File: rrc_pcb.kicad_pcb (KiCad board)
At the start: 2 copper layers, 148.8 x 62.4 mm, 20 parts, among them J1 Voltage Regulator Input, J2 Conn_01x03_Male, U1 ADXL357Z, U2 Teensy3.6-teensy, U3 BN220-GPS, U4 MS5611, U5 logo

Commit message: update 2
updated .sch added teensy4.1 , and updated footprints. Still in debugging stage
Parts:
- removed REF** (x7): MountingHole_2.1mm, MountingHole:MountingHole_2.1mm
- removed RF11: RFD900+-RF_Module, rfd900+:RFD900+
- added U6: logo, logo:RRC_logo, F.Cu at (152.4, 16.5)
- U1: value ADXL357Z -> iridium9602; footprint adxl357z:ADXL357 -> Connector_PinHeader_2.54mm:PinHeader_1x04_P2.54mm_Horizontal
- U2: value Teensy3.6-teensy -> DEV-16771; footprint teensy:Teensy35_36 -> teensy:Teensy41
- U4: value MS5611 -> ICM-20948; footprint ms5611:1x07 -> Connector_PinHeader_2.54mm:PinHeader_2x10_P2.54mm_Vertical
- U5: value logo -> MS5611; footprint logo:RRC_logo -> ms5611:1x07
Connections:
- R3 pad 1: Net-(R3-Pad1) -> SCL1
- R4 pad 1: Net-(R4-Pad1) -> SDA1
- U1 pad 2: unconnected-(U1-Pad2) -> TX2
- U1 pad 3: T_VCC -> RX2
- U1 pad 4: unconnected-(U1-Pad4) -> GND
- U2 pad 1: T_GND -> TX1
- U2 pad 11: Net-(RF11-Pad9) -> unconnected-(U2-Pad11)
- U2 pad 12: Net-(RF11-Pad7) -> unconnected-(U2-Pad12)
- U2 pad 15: T_VCC -> unconnected-(U2-Pad15)
- U2 pad 16: unconnected-(U2-Pad16) -> SCL1
- U2 pad 17: unconnected-(U2-Pad17) -> SDA1
- U2 pad 18: unconnected-(U2-Pad18) -> Net-(R2-Pad1)
- U2 pad 19: unconnected-(U2-Pad19) -> Net-(R1-Pad1)
- U2 pad 2: Net-(U2-Pad2) -> unconnected-(U2-Pad2)
- U2 pad 24: Net-(BZ1-Pad1) -> unconnected-(U2-Pad24)
- U2 pad 3: Net-(U2-Pad3) -> unconnected-(U2-Pad3)
- U2 pad 39: GND -> unconnected-(U2-Pad39)
- U2 pad 41: unconnected-(U2-Pad41) -> Net-(BZ1-Pad1)
- U2 pad 42: unconnected-(U2-Pad42) -> (no net)
- U2 pad 43: unconnected-(U2-Pad43) -> (no net)
- U2 pad 44: unconnected-(U2-Pad44) -> (no net)
- U2 pad 45: Net-(R2-Pad1) -> (no net)
- U2 pad 46: Net-(R1-Pad1) -> (no net)
- U2 pad 47: unconnected-(U2-Pad47) -> (no net)
- U2 pad 48: unconnected-(U2-Pad48) -> (no net)
- U2 pad 49: unconnected-(U2-Pad49) -> (no net)
- U2 pad 5: Net-(R3-Pad1) -> unconnected-(U2-Pad5)
- U2 pad 50: unconnected-(U2-Pad50) -> (no net)
- U2 pad 51: unconnected-(U2-Pad51) -> (no net)
- U2 pad 52: unconnected-(U2-Pad52) -> (no net)
- U2 pad 53: VCC -> (no net)
- U2 pad 54: unconnected-(U2-Pad54) -> (no net)
- U2 pad 55: unconnected-(U2-Pad55) -> (no net)
- U2 pad 56: unconnected-(U2-Pad56) -> (no net)
- U2 pad 57: unconnected-(U2-Pad57) -> (no net)
- U2 pad 6: Net-(R4-Pad1) -> unconnected-(U2-Pad6)
- U2 pad 7: unconnected-(U2-Pad7) -> RX2
- U2 pad 8: unconnected-(U2-Pad8) -> TX2
- U3 pad 2: Net-(U2-Pad3) -> TX1
- U3 pad 3: Net-(U2-Pad2) -> RX1
- U4 pad 1: T_VCC -> unconnected-(U4-Pad1)
- U4 pad 2: T_GND -> unconnected-(U4-Pad2)
- U4 pad 3: Net-(R3-Pad1) -> unconnected-(U4-Pad3)
- U4 pad 4: Net-(R4-Pad1) -> unconnected-(U4-Pad4)
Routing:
- net unconnected-(U2-Pad34): track 0.00 -> 163.4 mm
- net GND: track 163.4 -> 0.00 mm
- net unconnected-(U2-Pad11): track 0.00 -> 108.6 mm
- net Net-(RF11-Pad9): track 108.6 -> 0.00 mm
- net unconnected-(U2-Pad12): track 0.00 -> 108.5 mm
- net Net-(RF11-Pad7): track 108.5 -> 0.00 mm
- net Net-(BZ1-Pad1): track 84.5 -> 191.7 mm
- net Net-(R1-Pad1): track 107.2 -> 0.00 mm
- net SDA1: track 0.00 -> 94.0 mm
- net Net-(R4-Pad1): track 48.8 -> 0.00 mm
- net Net-(R3-Pad1): track 45.2 -> 0.00 mm
- net unconnected-(U2-Pad2): track 0.00 -> 25.8 mm, vias 0 -> 1
- net Net-(U2-Pad2): track 25.8 -> 0.00 mm, vias 1 -> 0
- net unconnected-(U2-Pad3): track 0.00 -> 25.3 mm
- net Net-(U2-Pad3): track 25.3 -> 0.00 mm
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
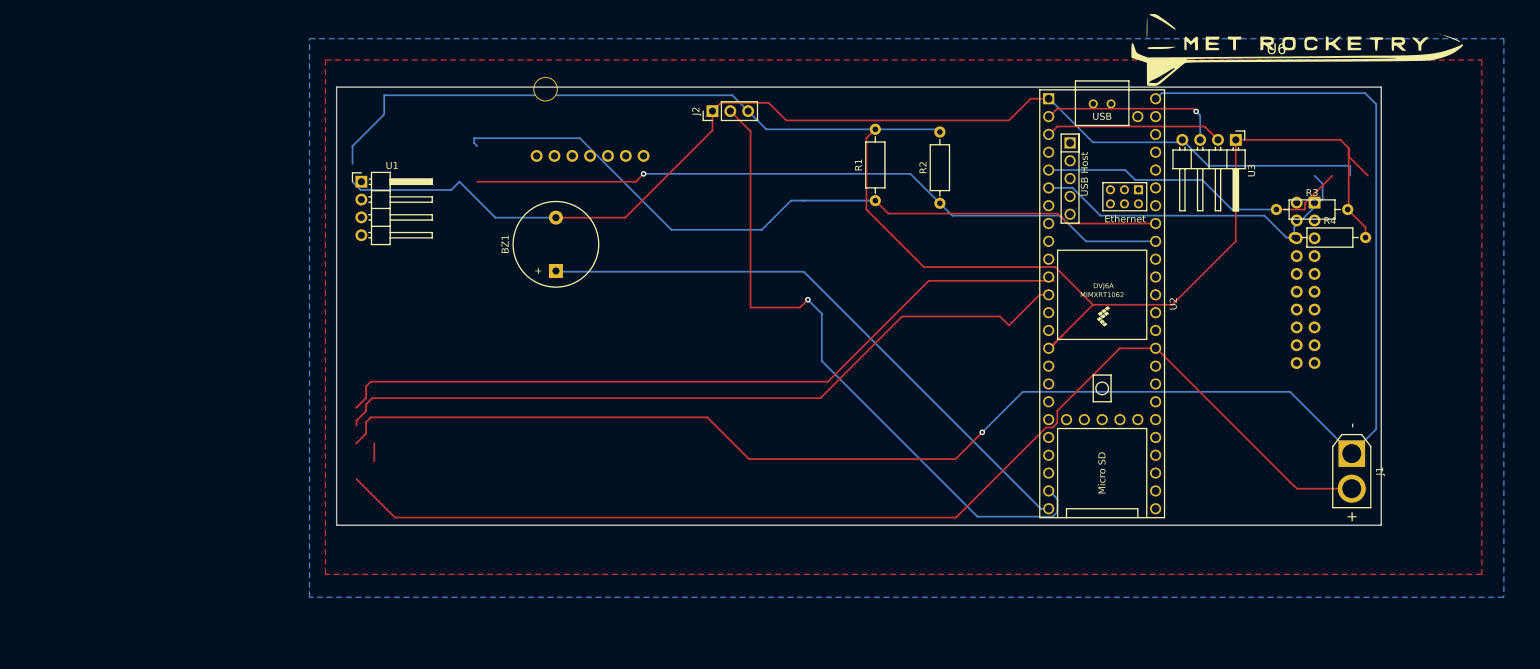
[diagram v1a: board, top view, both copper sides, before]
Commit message: updated pcb footprints
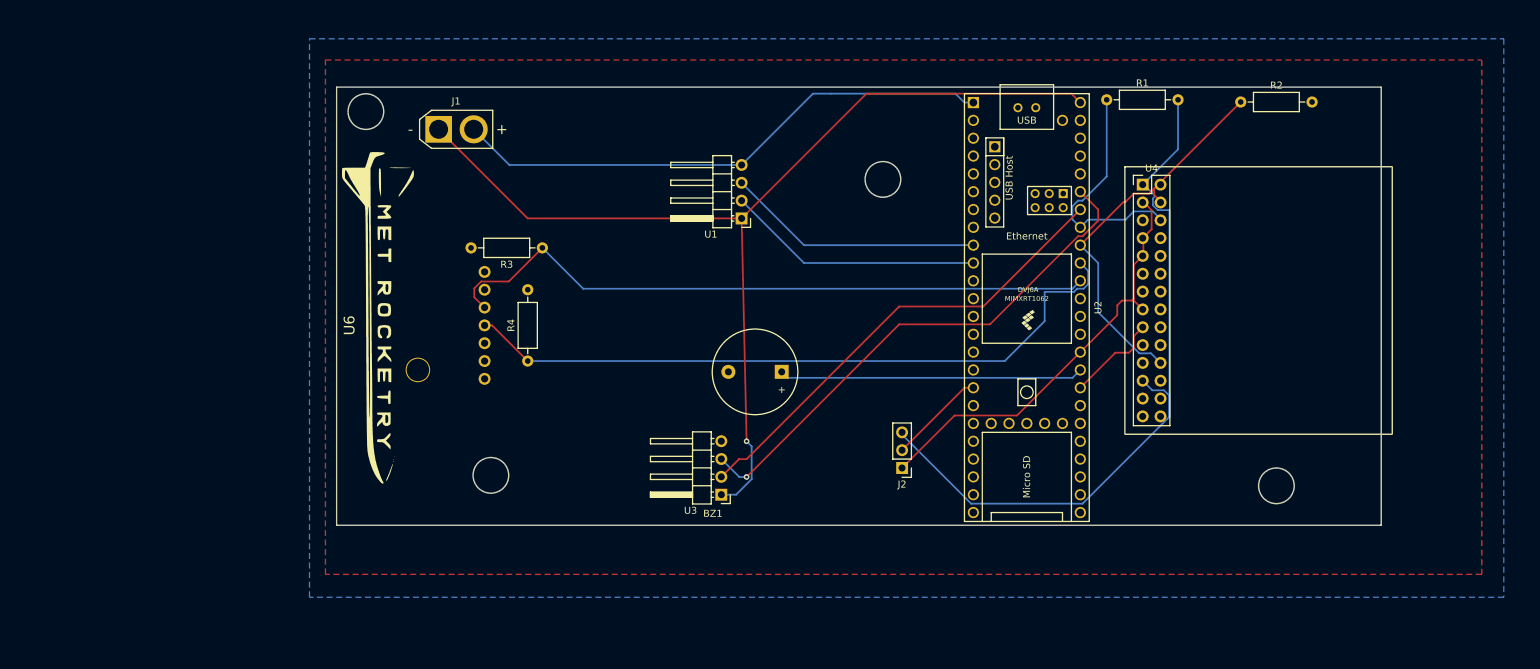
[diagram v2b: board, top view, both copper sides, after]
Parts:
- BZ1: value Buzzer -> Buzzer-Device
- J1: value Voltage Regulator Input -> Conn_01x02_Male-Connector
- J2: value Conn_01x03_Male -> Conn_01x03_Male-Connector
- R1, R2, R3, R4: value Pull up -> R-Device
- U2: value DEV-16771 -> Teensy4.1
- U4: value ICM-20948 -> ICM-20948; footprint Connector_PinHeader_2.54mm:PinHeader_2x10_P2.54mm_Vertical -> Connector_PinHeader_2.54mm:PinHeader_2x14_P2.54mm_Vertical; moved to F.Cu
- moved J1 138.1 mm to (33.0, 27.9), turned to 0 degrees
- moved U6 132.7 mm to (24.5, 51.9), turned to -90 degrees
- moved R4 110.6 mm to (45.7, 61.0), turned to 90 degrees
- moved R3 104.7 mm to (47.8, 44.8), turned to 180 degrees
- moved U3 89.1 mm to (73.3, 80.0), turned to 180 degrees
- moved J2 57.6 mm to (99.1, 76.2), turned to 180 degrees
- moved U1 54.4 mm to (76.2, 40.6), turned to 180 degrees
- moved R2 45.2 mm to (147.3, 24.1), turned to 0 degrees
- moved R1 36.0 mm to (128.2, 23.7), turned to 0 degrees
- moved BZ1 35.2 mm to (81.9, 62.5), turned to 180 degrees
- moved U4 24.6 mm to (133.3, 35.8), turned to 0 degrees
- moved U5 23.2 mm to (43.4, 55.9), turned to -90 degrees
- moved U2 10.7 mm to (116.8, 53.3)
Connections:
- R1 pad 1: Net-(R1-Pad1) -> SCL2
- R2 pad 1: Net-(R2-Pad1) -> SDA2
- U1 pad 1: T_VCC -> VCC
- U2 pad 1: TX1 -> GND
- U2 pad 10: unconnected-(U2-Pad10) -> TX2
- U2 pad 15: unconnected-(U2-Pad15) -> T_VCC
- U2 pad 16: SCL1 -> unconnected-(U2-Pad16)
- U2 pad 17: SDA1 -> Net-(J2-Pad2)
- U2 pad 18: Net-(R2-Pad1) -> unconnected-(U2-Pad18)
- U2 pad 19: Net-(R1-Pad1) -> unconnected-(U2-Pad19)
- U2 pad 23: Net-(J2-Pad2) -> unconnected-(U2-Pad23)
- U2 pad 32: unconnected-(U2-Pad32) -> INT1
- U2 pad 33: unconnected-(U2-Pad33) -> Net-(BZ1-Pad1)
- U2 pad 34: unconnected-(U2-Pad34) -> T_GND
- U2 pad 38: unconnected-(U2-Pad38) -> SCL1
- U2 pad 39: unconnected-(U2-Pad39) -> SDA1
- U2 pad 40: unconnected-(U2-Pad40) -> SDA2
- U2 pad 41: Net-(BZ1-Pad1) -> SCL2
- U2 pad 42: (no net) -> TX1
- U2 pad 43: (no net) -> RX1
- U2 pad 44: (no net) -> unconnected-(U2-Pad44)
- U2 pad 45: (no net) -> unconnected-(U2-Pad45)
- U2 pad 46: (no net) -> unconnected-(U2-Pad46)
- U2 pad 47: (no net) -> unconnected-(U2-Pad47)
- U2 pad 48: (no net) -> VCC
- U2 pad 49: (no net) -> unconnected-(U2-Pad49)
- U2 pad 50: (no net) -> unconnected-(U2-Pad50)
- U2 pad 51: (no net) -> unconnected-(U2-Pad51)
- U2 pad 52: (no net) -> unconnected-(U2-Pad52)
- U2 pad 53: (no net) -> unconnected-(U2-Pad53)
- U2 pad 54: (no net) -> unconnected-(U2-Pad54)
- U2 pad 55: (no net) -> unconnected-(U2-Pad55)
- U2 pad 56: (no net) -> unconnected-(U2-Pad56)
- U2 pad 57: (no net) -> unconnected-(U2-Pad57)
- U2 pad 58: (no net) -> unconnected-(U2-Pad58)
- U2 pad 59: (no net) -> unconnected-(U2-Pad59)
- U2 pad 60: (no net) -> unconnected-(U2-Pad60)
- U2 pad 61: (no net) -> unconnected-(U2-Pad61)
- U2 pad 62: (no net) -> unconnected-(U2-Pad62)
- U2 pad 63: (no net) -> unconnected-(U2-Pad63)
- U2 pad 64: (no net) -> unconnected-(U2-Pad64)
- U2 pad 65: (no net) -> unconnected-(U2-Pad65)
- U2 pad 66: (no net) -> unconnected-(U2-Pad66)
- U2 pad 67: (no net) -> unconnected-(U2-Pad67)
- U2 pad 7: RX2 -> unconnected-(U2-Pad7)
- U2 pad 8: TX2 -> unconnected-(U2-Pad8)
- U2 pad 9: unconnected-(U2-Pad9) -> RX2
- U3 pad 1: T_VCC -> VCC
- U4 pad 13: T_VCC -> unconnected-(U4-Pad13)
- U4 pad 15: unconnected-(U4-Pad15) -> T_GND
- U4 pad 17: unconnected-(U4-Pad17) -> T_GND
- U4 pad 18: T_GND -> unconnected-(U4-Pad18)
- U4 pad 19: T_GND -> unconnected-(U4-Pad19)
- U4 pad 20: T_GND -> SCL2
- U4 pad 7: unconnected-(U4-Pad7) -> INT1
- U4 pad 8: T_VCC -> unconnected-(U4-Pad8)
- U4 pad 9: unconnected-(U4-Pad9) -> (no net)
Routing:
- net unconnected-(U2-Pad34): track 163.4 -> 0.00 mm
- net Net-(BZ1-Pad1): track 191.7 -> 43.4 mm
- net T_VCC: track 228.3 -> 105.3 mm
- net unconnected-(U2-Pad11): track 108.6 -> 0.00 mm
- net unconnected-(U2-Pad12): track 108.5 -> 0.00 mm
- net Net-(R2-Pad1): track 101.2 -> 0.00 mm, vias 1 -> 0
- net T_GND: track 161.6 -> 61.2 mm
- net SCL1: track 0.00 -> 95.0 mm
- net VCC: track 237.9 -> 147.3 mm
- net Net-(J2-Pad2): track 93.9 -> 13.8 mm, vias 1 -> 0
- net GND: track 0.00 -> 78.0 mm
- net RX1: track 0.00 -> 75.1 mm, vias 0 -> 1
- net TX1: track 0.00 -> 66.9 mm
- net SDA2: track 0.00 -> 56.1 mm
- net TX2: track 0.00 -> 36.7 mm
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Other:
- outline, holes or cut-outs redrawn

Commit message: optimized and finalized pcb
reduced sizing and fixed traces.
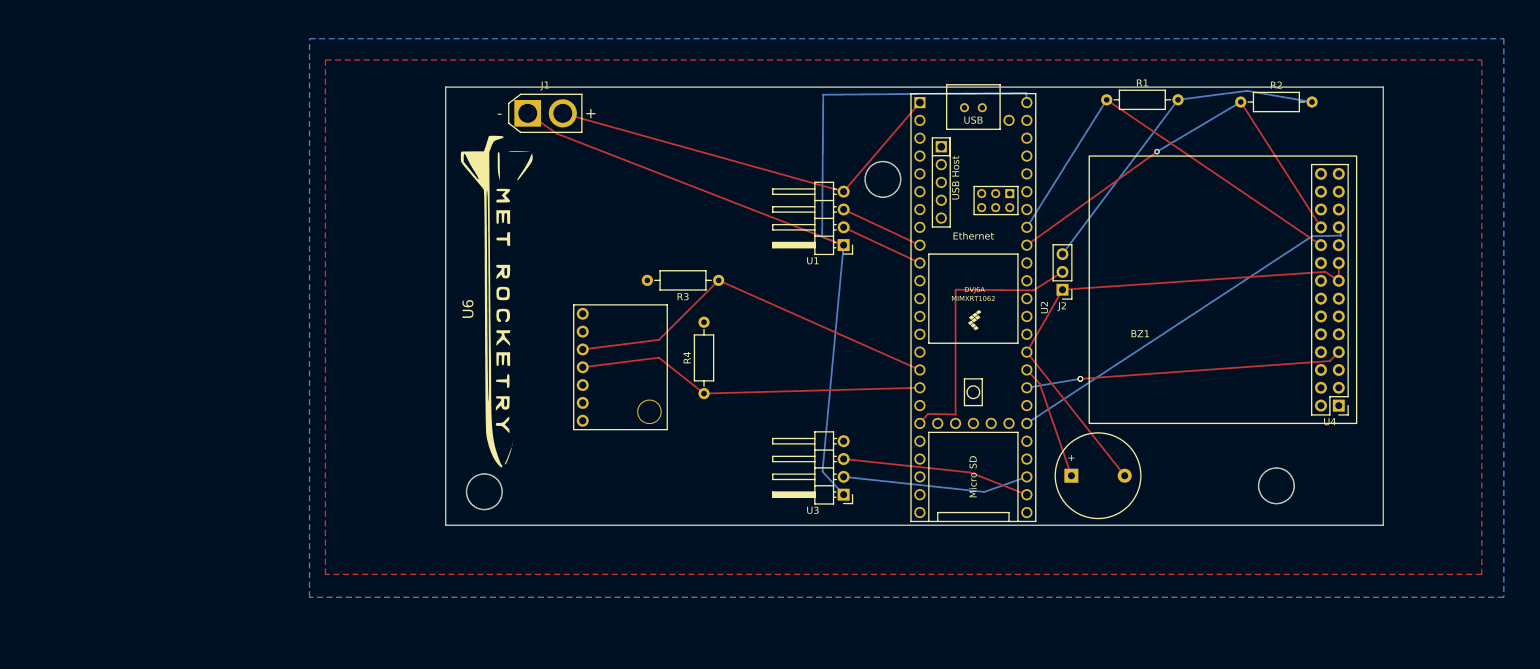
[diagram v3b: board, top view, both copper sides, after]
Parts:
- U5: moved to F.Cu
- moved BZ1 43.9 mm to (123.2, 77.3), turned to 0 degrees
- moved U4 42.1 mm to (161.3, 67.3), turned to 180 degrees
- moved J2 34.2 mm to (121.9, 50.8)
- moved R3 25.5 mm to (72.9, 49.5)
- moved R4 25.5 mm to (70.8, 65.6)
- moved U3 17.4 mm to (90.7, 80.0)
- moved U6 17.1 mm to (41.4, 49.5)
- moved U1 15.0 mm to (90.7, 44.4)
- moved J1 12.9 mm to (45.7, 25.7)
- moved U5 8.70 mm to (49.7, 61.8)
- moved U2 7.62 mm to (109.2, 53.3)
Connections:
- J2 pad 2: Net-(J2-Pad2) -> Net-(U2-Pad19)
- U2 pad 16: unconnected-(U2-Pad16) -> SCL1
- U2 pad 17: Net-(J2-Pad2) -> SDA1
- U2 pad 19: unconnected-(U2-Pad19) -> Net-(U2-Pad19)
- U2 pad 26: unconnected-(U2-Pad26) -> RX1
- U2 pad 27: unconnected-(U2-Pad27) -> TX1
- U2 pad 30: unconnected-(U2-Pad30) -> FSYNC
- U2 pad 38: SCL1 -> unconnected-(U2-Pad38)
- U2 pad 39: SDA1 -> unconnected-(U2-Pad39)
- U2 pad 42: TX1 -> unconnected-(U2-Pad42)
- U2 pad 43: RX1 -> unconnected-(U2-Pad43)
- U4 pad 21: T_GND -> FSYNC
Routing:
- net T_VCC: track 105.3 -> 46.8 mm
- net FSYNC: track 0.00 -> 54.0 mm
- net SDA1: track 98.6 -> 49.9 mm
- net RX1: track 75.1 -> 26.8 mm, vias 1 -> 0
- net SCL1: track 95.0 -> 54.3 mm
- net TX1: track 66.9 -> 26.6 mm
- net Net-(U2-Pad19): track 0.00 -> 39.5 mm
- net INT1: track 13.6 -> 45.2 mm, vias 0 -> 2
- net Net-(BZ1-Pad1): track 43.4 -> 16.6 mm
- net TX2: track 36.7 -> 12.0 mm
- net RX2: track 36.7 -> 12.0 mm
- net SCL2: track 34.0 -> 58.3 mm
- net GND: track 78.0 -> 58.2 mm
- net T_GND: track 61.2 -> 75.1 mm
- net Net-(J2-Pad2): track 13.8 -> 0.00 mm
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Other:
- board size 148.8 x 62.4 mm -> 133.6 x 62.4 mm

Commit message: added edge cuts and mounting holes
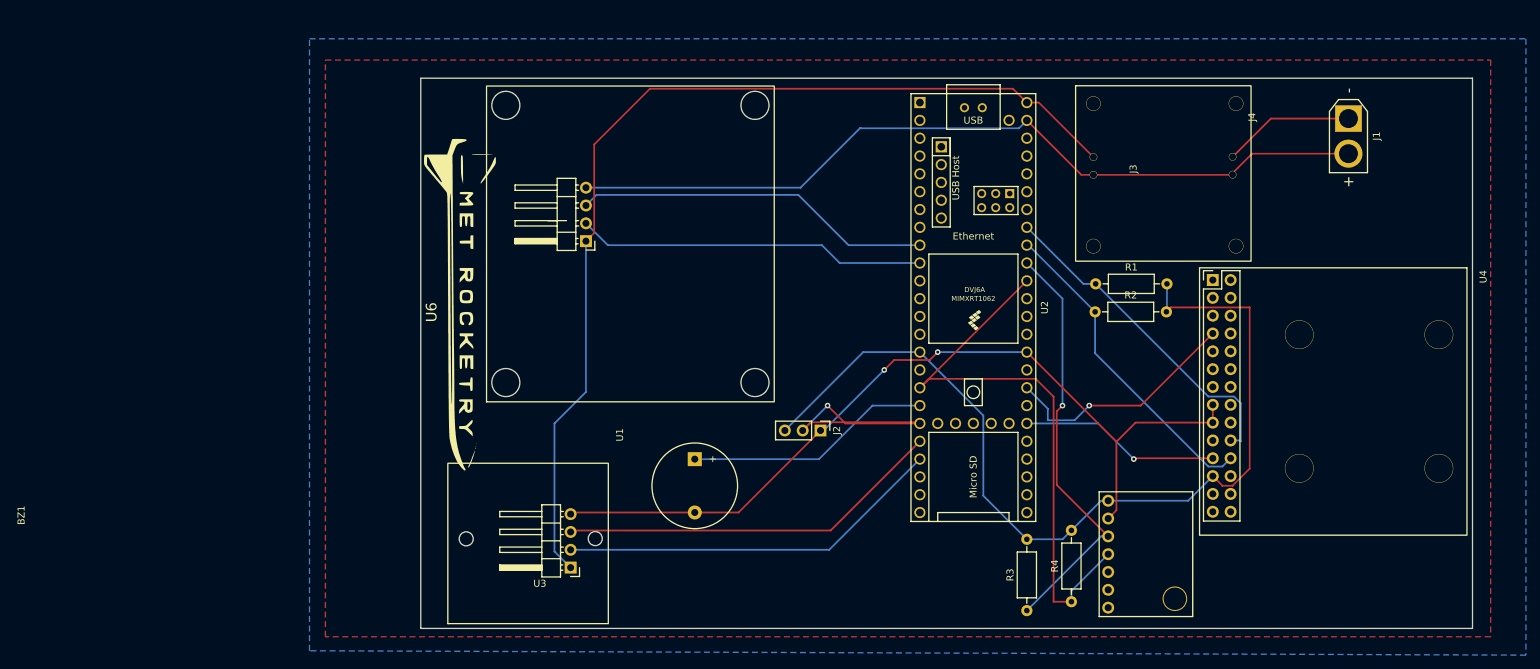
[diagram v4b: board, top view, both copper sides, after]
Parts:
- added J3: Conn_01x02_Male-Connector, Connector_PinSocket_2.54mm:PinSocket_1x02_P2.54mm_Horizontal, F.Cu at (123.8, 21.7)
- added J4: Conn_01x02_Female, Connector_PinSocket_2.54mm:PinSocket_2x01_P2.54mm_Horizontal, F.Cu at (146.2, 31.9)
- moved J1 116.9 mm to (162.7, 26.4), turned to -90 degrees
- moved U5 79.5 mm to (124.6, 88.5)
- moved R3 64.4 mm to (116.8, 96.5), turned to 90 degrees
- moved R4 60.2 mm to (123.2, 95.2)
- moved U3 59.3 mm to (34.3, 98.4), turned to 90 degrees
- moved U1 55.6 mm to (39.8, 66.8), turned to 90 degrees
- moved BZ1 53.7 mm to (69.5, 74.9), turned to -90 degrees
- moved J2 39.9 mm to (87.4, 70.9), turned to -90 degrees
- moved R2 36.4 mm to (126.6, 54.0)
- moved U4 26.8 mm to (179.5, 47.7), turned to -90 degrees
- moved R1 26.3 mm to (126.6, 50.0)
- moved U6 5.26 mm to (36.2, 50.0)
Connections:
- J1 pad 1: VCC -> 7.2V
- U2 pad 1: GND -> unconnected-(U2-Pad1)
- U2 pad 16: SCL1 -> unconnected-(U2-Pad16)
- U2 pad 18: unconnected-(U2-Pad18) -> Net-(BZ1-Pad1)
- U2 pad 20: unconnected-(U2-Pad20) -> RX1
- U2 pad 21: unconnected-(U2-Pad21) -> TX1
- U2 pad 26: RX1 -> unconnected-(U2-Pad26)
- U2 pad 27: TX1 -> unconnected-(U2-Pad27)
- U2 pad 33: Net-(BZ1-Pad1) -> unconnected-(U2-Pad33)
- U2 pad 38: unconnected-(U2-Pad38) -> SDA1
- U2 pad 39: unconnected-(U2-Pad39) -> SCL1
- U2 pad 47: unconnected-(U2-Pad47) -> GND
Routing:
- net T_VCC: track 46.8 -> 133.0 mm
- net GND: track 58.2 -> 117.1 mm
- net T_GND: track 75.1 -> 121.5 mm, vias 0 -> 2
- net RX2: track 12.0 -> 51.2 mm
- net TX2: track 12.0 -> 49.9 mm
- net SDA1: track 49.9 -> 82.9 mm
- net TX1: track 26.6 -> 55.1 mm
- net RX1: track 26.8 -> 55.1 mm
- net FSYNC: track 54.0 -> 28.6 mm, vias 0 -> 1
- net 7.2V: track 0.00 -> 18.8 mm
- net Net-(BZ1-Pad1): track 16.6 -> 35.2 mm
- net SDA2: track 57.9 -> 46.1 mm, vias 1 -> 0
- net INT1: track 45.2 -> 34.5 mm, vias 2 -> 1
- net SCL2: track 58.3 -> 47.8 mm
- net SCL1: track 54.3 -> 60.4 mm, vias 0 -> 1
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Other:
- board size 133.6 x 62.4 mm -> 149.9 x 78.4 mm
